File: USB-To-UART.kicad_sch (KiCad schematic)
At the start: 1 part, among them U4 CH340E

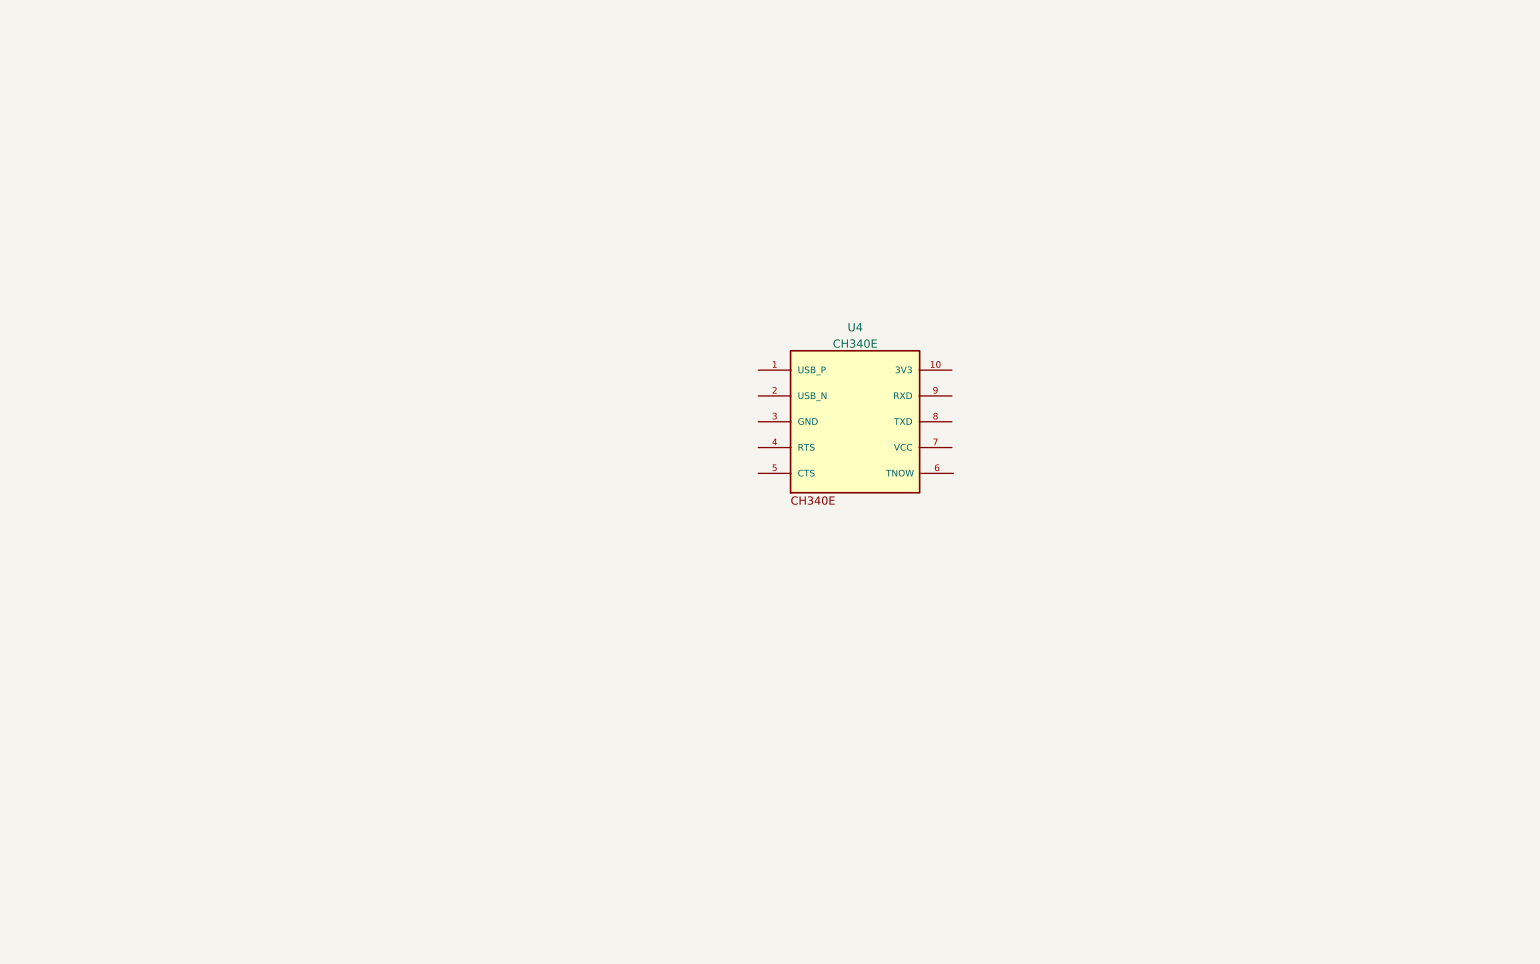
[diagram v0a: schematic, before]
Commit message: Made USB-To-UART connections
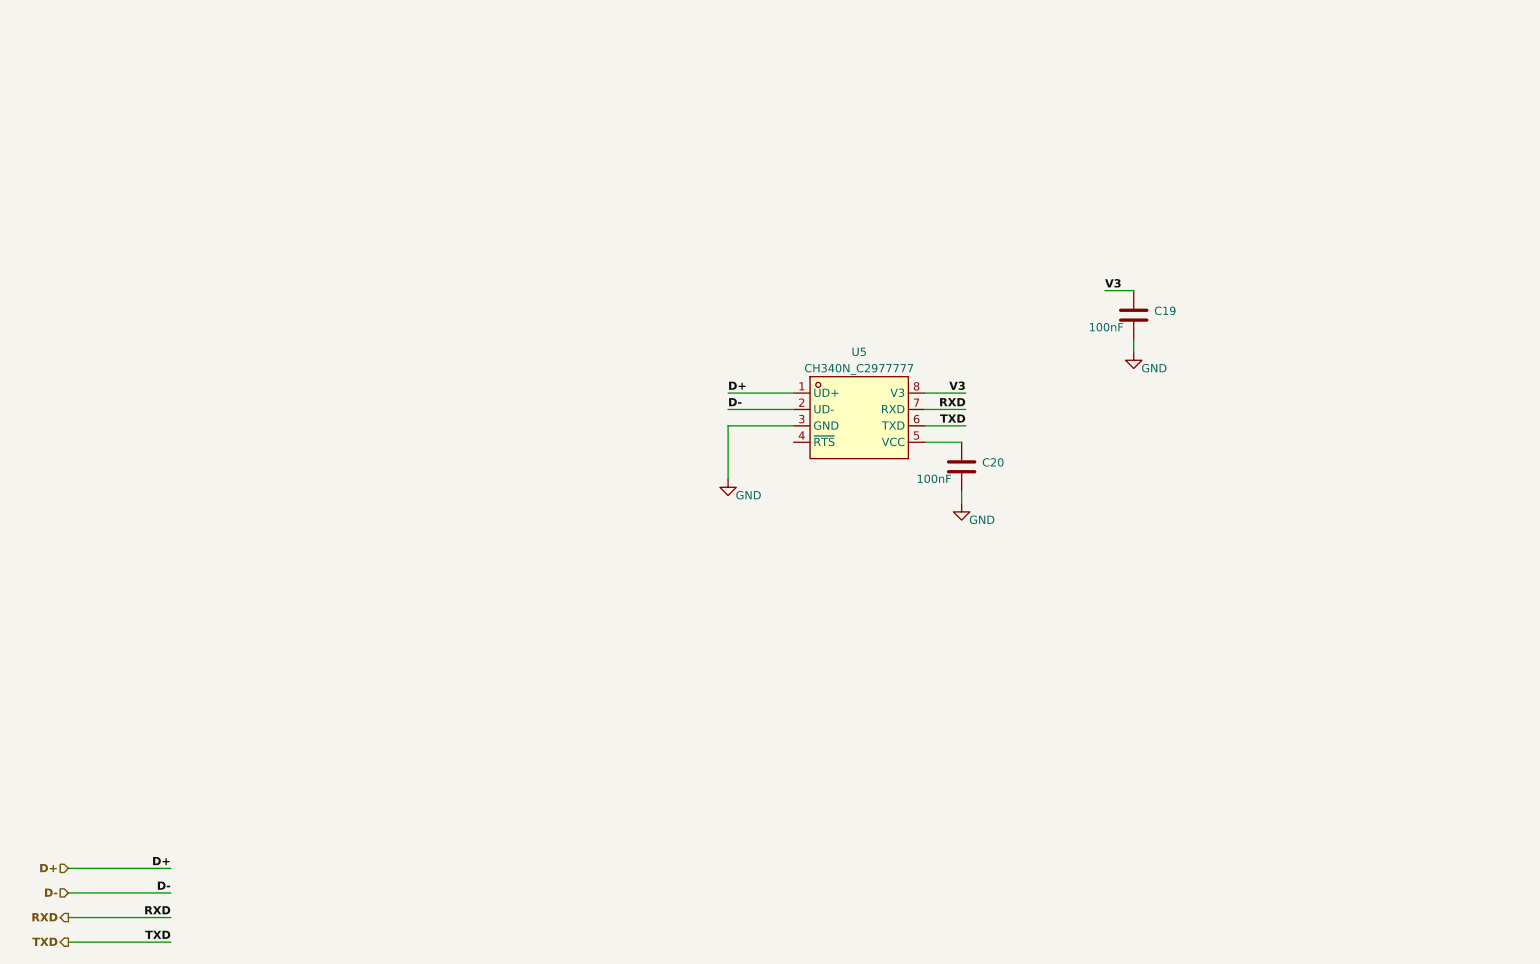
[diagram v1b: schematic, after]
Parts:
- removed U4: CH340E, CH340E:MSOP-10, symbol ESP32-S3_DB:CH340E
- added C19, C20: 100nF, symbol ESP32-S3_DB:C
- added U5: CH340N_C2977777, easyeda2kicad:SOP-8_L4.9-W3.9-P1.27-LS6.0-BL, symbol ESP32-S3_DB:CH340N_C2977777
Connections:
- new net: C20.2, U5.5 (VCC)
- new net D+: U5.1 (UD+)
- new net D-: U5.2 (UD-)
- new net GND: C19.1, C20.1, U5.3 (GND)
- new net RXD: U5.7 (RXD)
- new net TXD: U5.6 (TXD)
- new net V3: C19.2, U5.8 (V3)

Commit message: Added RS-485 Transceiver
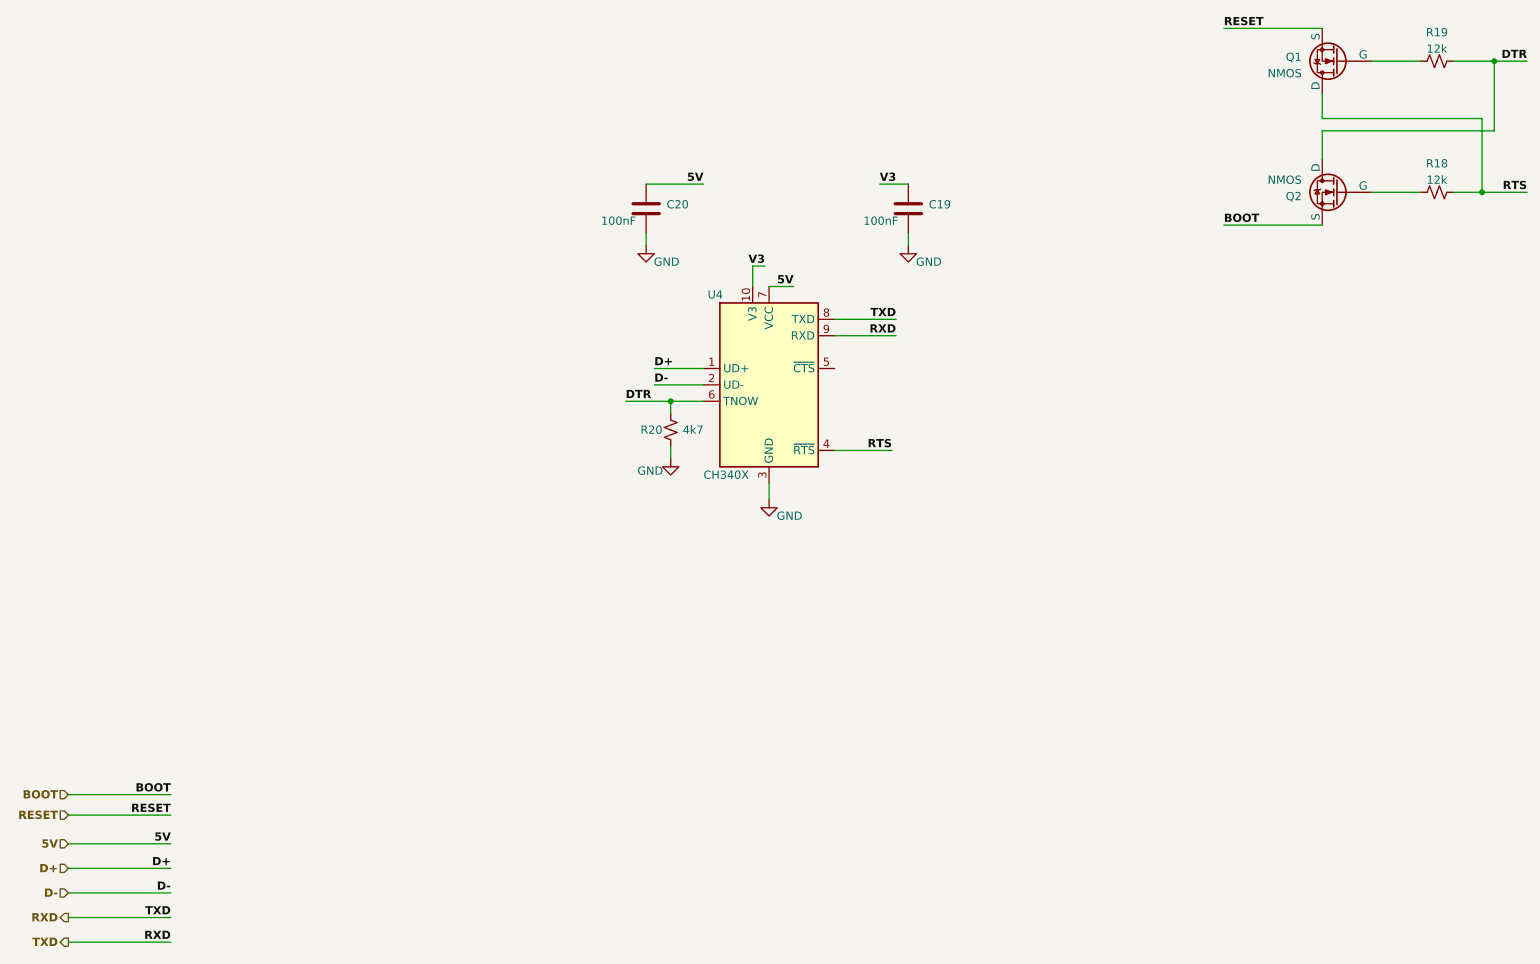
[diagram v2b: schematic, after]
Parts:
- removed U5: CH340N_C2977777, easyeda2kicad:SOP-8_L4.9-W3.9-P1.27-LS6.0-BL, symbol ESP32-S3_DB:CH340N_C2977777
- added Q1, Q2: NMOS, symbol ESP32-S3_DB:NMOS
- added R18, R19: 12k, symbol ESP32-S3_DB:R_Small_US
- added R20: 4k7, symbol ESP32-S3_DB:R_Small_US
- added U4: CH340X, Package_SO:MSOP-10_3x3mm_P0.5mm, symbol ESP32-S3_DB:CH340X
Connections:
- net D+: now also U4.1 (UD+)
- net D-: now also U4.2 (UD-)
- net GND: now also R20.1, U4.3 (GND)
- net RXD: now also U4.8 (TXD), U4.9 (RXD)
- net V3: now also U4.10 (V3)
- net 5V: now reaches C20.2
- net 5V: now also U4.7 (VCC)
- new net: Q2.2 (G), R18.1
- new net: Q1.2 (G), R19.1
- new net BOOT: Q2.3 (S)
- new net DTR: Q2.1 (D), R19.2, R20.2, U4.6 (TNOW)
- new net RESET: Q1.3 (S)
- new net RTS: Q1.1 (D), R18.2, U4.4 (~{RTS})
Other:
- moved on the sheet: C19, C20
